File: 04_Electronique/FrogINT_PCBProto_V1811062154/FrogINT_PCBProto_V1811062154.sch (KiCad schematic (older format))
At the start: 35 parts, among them IC1 TTP223-BA6, J1 USB_B_Mini, J2 Conn_01x01_Female, J3 AVR-JTAG-10, Q1 PMV48XP, Q2 PMV48XP, U1 NCP1117-5.0_SOT223, U2 LP2985-3.3, U3 ATmega16U4RC-AU, Y1 16MHz

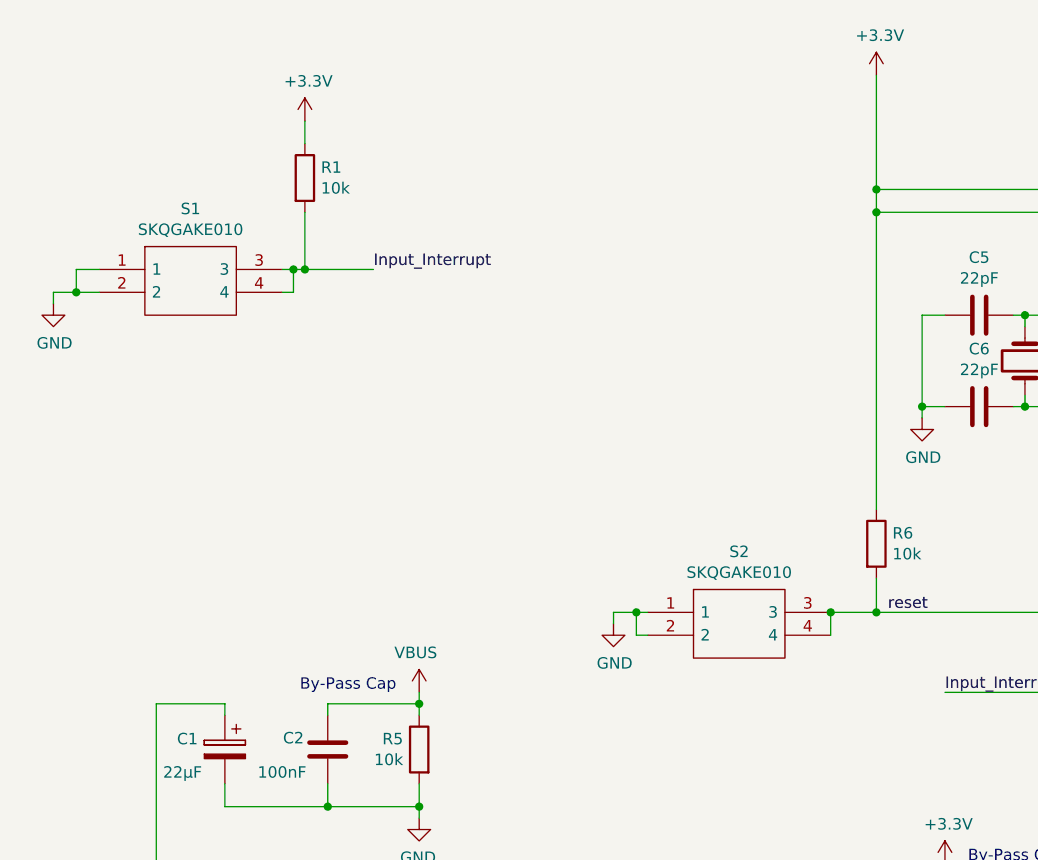
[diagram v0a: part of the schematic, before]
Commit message: 12/02/2019 : Remplacement des gros boutons par des plus petits
Impact :
	Mise à jour du fichier Excel FrogINT_BOM_V03-Commit-22-01-2019_RFQ_RS.xlsx suite à la mise à jour de la BOM (Attention pour les chiffrage en cours)
	Création des fichiers sources mécaniques pour ce nouveau Switch_PTS810SJG250SMTRLFS
	Mise à jour des références des librairies (pointeur).
	Déplacement partiel de la librairie SamacSys_Parts directement dans la "racine" du projet (et non plus dans l'arborescence C: etc.)
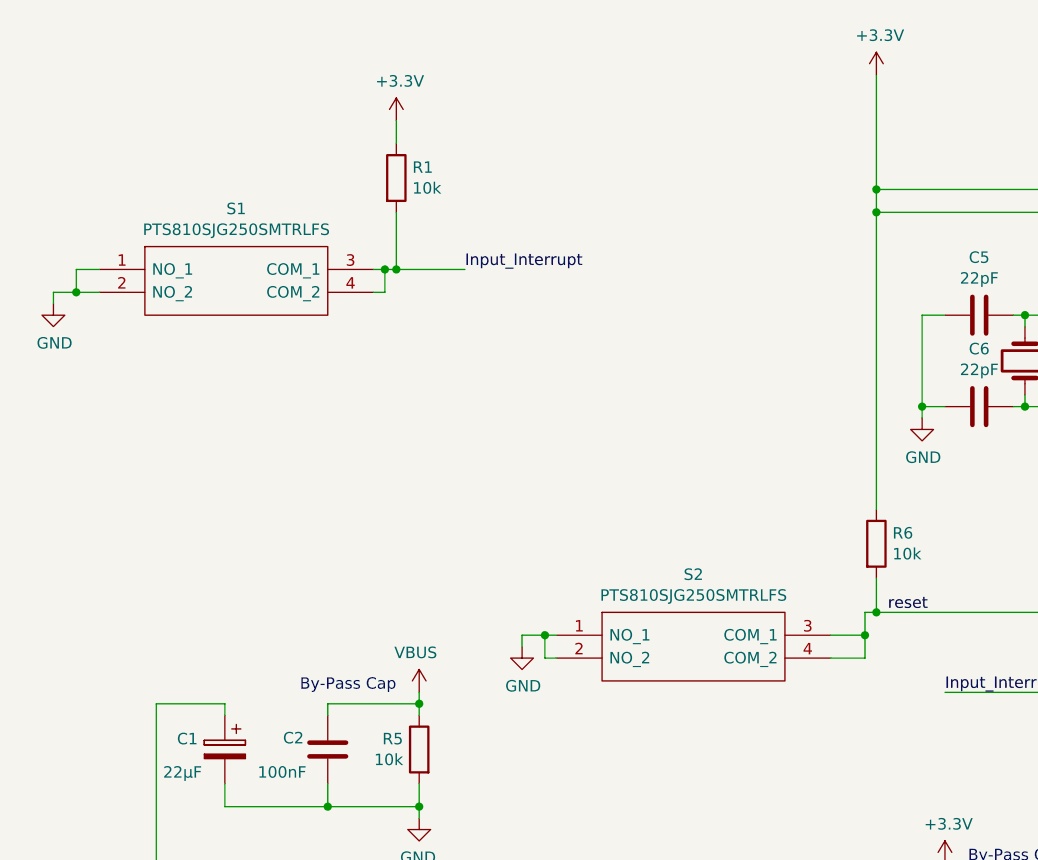
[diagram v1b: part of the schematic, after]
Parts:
- removed S1, S2: SKQGAKE010, SamacSys_Parts:SKQGAKE010, symbol FrogINT_PCBProto_V1811062154-rescue:SKQGAKE010-SamacSys_Parts
- added S1, S2: PTS810SJG250SMTRLFS, SamacSys_Parts:PTS810SJG250SMTRLFS, symbol SamacSys_Parts:PTS810SJG250SMTRLFS
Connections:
- net GND: now also S1.1 (NO_1), S1.2 (NO_2), S2.1 (NO_1), S2.2 (NO_2)
- net Input_Interrupt: now also S1.3 (COM_1), S1.4 (COM_2)
- net reset: now also S2.3 (COM_1), S2.4 (COM_2)
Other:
- moved on the sheet: R1
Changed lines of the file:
@@
 L power:GND #PWR012
 U 1 1 5BE239E3
-P 3200 3300
-F 0 "#PWR012" H 3200 3050 50  0001 C CNN
-F 1 "GND" H 3205 3127 50  0000 C CNN
-F 2 "" H 3200 3300 50  0001 C CNN
-F 3 "" H 3200 3300 50  0001 C CNN
-	1    3200 3300
-	1    0    0    -1
-$EndComp
-Wire Wire Line
-	3200 3300 3200 3250
-Wire Wire Line
-	3200 3250 3300 3250
+P 2800 3400
+F 0 "#PWR012" H 2800 3150 50  0001 C CNN
+F 1 "GND" H 2805 3227 50  0000 C CNN
+F 2 "" H 2800 3400 50  0001 C CNN
+F 3 "" H 2800 3400 50  0001 C CNN
+	1    2800 3400
+	1    0    0    -1
+$EndComp
+Wire Wire Line
+	2800 3400 2800 3350
+Wire Wire Line
+	2800 3350 2900 3350
 $Comp
 L Device:R R6
@@
 	5900 4800 5900 4750
 Wire Wire Line
-	4150 3250 4350 3250
-Wire Wire Line
 	4350 3100 4350 3250
-Connection ~ 4350 3250
 Wire Wire Line
 	4350 3250 5400 3250
@@
 L Device:R R1
 U 1 1 5BEA062B
-P 1850 1350
-F 0 "R1" H 1920 1396 50  0000 L CNN
-F 1 "10k" H 1920 1305 50  0000 L CNN
-F 2 "FTA_FrogINT_Library_Footprint_Package:R_0603_1608Metric" V 1780 1350 50  0001 C CNN
-F 3 "~" H 1850 1350 50  0001 C CNN
-	1    1850 1350
+P 2250 1350
+F 0 "R1" H 2320 1396 50  0000 L CNN
+F 1 "10k" H 2320 1305 50  0000 L CNN
+F 2 "FTA_FrogINT_Library_Footprint_Package:R_0603_1608Metric" V 2180 1350 50  0001 C CNN
+F 3 "~" H 2250 1350 50  0001 C CNN
+	1    2250 1350
 	1    0    0    -1
 $EndComp
@@
 L power:+3.3V #PWR04
 U 1 1 5BEA067C
-P 1850 1100
-F 0 "#PWR04" H 1850 950 50  0001 C CNN
-F 1 "+3.3V" H 1865 1273 50  0000 C CNN
-F 2 "" H 1850 1100 50  0001 C CNN
-F 3 "" H 1850 1100 50  0001 C CNN
-	1    1850 1100
-	1    0    0    -1
-$EndComp
-Wire Wire Line
-	1850 1100 1850 1200
-Wire Wire Line
-	1850 1500 1850 1750
+P 2250 1100
+F 0 "#PWR04" H 2250 950 50  0001 C CNN
+F 1 "+3.3V" H 2265 1273 50  0000 C CNN
+F 2 "" H 2250 1100 50  0001 C CNN
+F 3 "" H 2250 1100 50  0001 C CNN
+	1    2250 1100
+	1    0    0    -1
+$EndComp
+Wire Wire Line
+	2250 1100 2250 1200
+Wire Wire Line
+	2250 1500 2250 1750
 Text Label 4650 3600 0    50   ~ 0
 Input_Interrupt
 Wire Wire Line
 	5500 3600 4650 3600
-Text Label 2150 1750 0    50   ~ 0
+Text Label 2550 1750 0    50   ~ 0
 Input_Interrupt
 Wire Wire Line
-	1850 1750 2150 1750
+	2250 1750 2550 1750
 Wire Wire Line
 	6600 4350 9500 4350
@@
 $EndComp
 NoConn ~ 6600 2950
-$Comp
-L FrogINT_PCBProto_V1811062154-rescue:SKQGAKE010-SamacSys_Parts S1
-U 1 1 5C3DDA07
+Wire Wire Line
+	750  1850 850  1850
+Wire Wire Line
+	950  1750 850  1750
+Wire Wire Line
+	850  1750 850  1850
+Wire Wire Line
+	850  1850 950  1850
+Wire Wire Line
+	2250 1750 2200 1750
+Connection ~ 2250 1750
+Wire Wire Line
+	2150 1850 2200 1850
+Wire Wire Line
+	2200 1850 2200 1750
+Connection ~ 2200 1750
+Wire Wire Line
+	2200 1750 2150 1750
+Wire Wire Line
+	2950 3450 2900 3450
+Wire Wire Line
+	2900 3450 2900 3350
+Connection ~ 2900 3350
+Wire Wire Line
+	2900 3350 2950 3350
+$Comp
+L SamacSys_Parts:PTS810SJG250SMTRLFS S1
+U 1 1 5C636FCC
 P 950 1750
-F 0 "S1" H 1350 2015 50  0000 C CNN
-F 1 "SKQGAKE010" H 1350 1924 50  0000 C CNN
-F 2 "SamacSys_Parts:SKQGAKE010" H 1600 1850 50  0001 L CNN
-F 3 "http://uk.rs-online.com/webdocs/10d6/0900766b810d6137.pdf" H 1600 1750 50  0001 L CNN
-F 4 "Tact switch,SMT,SPST,with stem,3.43N o/f Stem Tactile Switch, SPST-NO 50 mA 1.5mm" H 1600 1650 50  0001 L CNN "Description"
-F 5 "" H 1600 1550 50  0001 L CNN "Height"
-F 6 "ALPS" H 1600 1450 50  0001 L CNN "Manufacturer_Name"
-F 7 "SKQGAKE010" H 1600 1350 50  0001 L CNN "Manufacturer_Part_Number"
-F 8 "7582076P" H 1600 1250 50  0001 L CNN "RS Part Number"
-F 9 "http://uk.rs-online.com/web/p/products/7582076P" H 1600 1150 50  0001 L CNN "RS Price/Stock"
-F 10 "688-SKQGAKE010" H 1600 1050 50  0001 L CNN "Mouser Part Number"
-F 11 "https://www.mouser.com/Search/Refine.aspx?Keyword=688-SKQGAKE010" H 1600 950 50  0001 L CNN "Mouser Price/Stock"
+F 0 "S1" H 1550 2015 50  0000 C CNN
+F 1 "PTS810SJG250SMTRLFS" H 1550 1924 50  0000 C CNN
+F 2 "SamacSys_Parts:PTS810SJG250SMTRLFS" H 2000 1850 50  0001 L CNN
+F 3 "https://www.ckswitches.com/media/1476/pts810.pdf" H 2000 1750 50  0001 L CNN
+F 4 "PTS810SJG250SMTRLFS (Tactile Switches) Switch Tactile N.O. SPST Button J-Bend 0.05A 16VDC 100000Cycles 3.92N SMD T/R" H 2000 1650 50  0001 L CNN "Description"
+F 5 "C & K COMPONENTS" H 2000 1450 50  0001 L CNN "Manufacturer_Name"
+F 6 "PTS810SJG250SMTRLFS" H 2000 1350 50  0001 L CNN "Manufacturer_Part_Number"
+F 7 "135-9492" H 2000 1250 50  0001 L CNN "RS Part Number"
+F 8 "611-PTS810SJG250SMTR" H 2000 1050 50  0001 L CNN "Mouser Part Number"
+F 9 "https://www.mouser.com/Search/Refine.aspx?Keyword=611-PTS810SJG250SMTR" H 2000 950 50  0001 L CNN "Mouser Price/Stock"
 	1    950  1750
 	1    0    0    -1
 $EndComp
-$Comp
-L FrogINT_PCBProto_V1811062154-rescue:SKQGAKE010-SamacSys_Parts S2
-U 1 1 5C3DDAF3
-P 3350 3250
-F 0 "S2" H 3750 3515 50  0000 C CNN
-F 1 "SKQGAKE010" H 3750 3424 50  0000 C CNN
-F 2 "SamacSys_Parts:SKQGAKE010" H 4000 3350 50  0001 L CNN
-F 3 "http://uk.rs-online.com/webdocs/10d6/0900766b810d6137.pdf" H 4000 3250 50  0001 L CNN
-F 4 "Tact switch,SMT,SPST,with stem,3.43N o/f Stem Tactile Switch, SPST-NO 50 mA 1.5mm" H 4000 3150 50  0001 L CNN "Description"
-F 5 "" H 4000 3050 50  0001 L CNN "Height"
-F 6 "ALPS" H 4000 2950 50  0001 L CNN "Manufacturer_Name"
-F 7 "SKQGAKE010" H 4000 2850 50  0001 L CNN "Manufacturer_Part_Number"
-F 8 "7582076P" H 4000 2750 50  0001 L CNN "RS Part Number"
-F 9 "http://uk.rs-online.com/web/p/products/7582076P" H 4000 2650 50  0001 L CNN "RS Price/Stock"
-F 10 "688-SKQGAKE010" H 4000 2550 50  0001 L CNN "Mouser Part Number"
-F 11 "https://www.mouser.com/Search/Refine.aspx?Keyword=688-SKQGAKE010" H 4000 2450 50  0001 L CNN "Mouser Price/Stock"
-	1    3350 3250
-	1    0    0    -1
-$EndComp
-Wire Wire Line
-	750  1850 850  1850
-Wire Wire Line
-	950  1750 850  1750
-Wire Wire Line
-	850  1750 850  1850
 Connection ~ 850  1850
-Wire Wire Line
-	850  1850 950  1850
-Wire Wire Line
-	1850 1750 1800 1750
-Connection ~ 1850 1750
-Wire Wire Line
-	1750 1850 1800 1850
-Wire Wire Line
-	1800 1850 1800 1750
-Connection ~ 1800 1750
-Wire Wire Line
-	1800 1750 1750 1750
-Wire Wire Line
-	4150 3350 4150 3250
-Connection ~ 4150 3250
-Wire Wire Line
-	3350 3350 3300 3350
-Wire Wire Line
-	3300 3350 3300 3250
-Connection ~ 3300 3250
-Wire Wire Line
-	3300 3250 3350 3250
+$Comp
+L SamacSys_Parts:PTS810SJG250SMTRLFS S2
+U 1 1 5C64EBFD
+P 2950 3350
+F 0 "S2" H 3550 3615 50  0000 C CNN
+F 1 "PTS810SJG250SMTRLFS" H 3550 3524 50  0000 C CNN
+F 2 "SamacSys_Parts:PTS810SJG250SMTRLFS" H 4000 3450 50  0001 L CNN
+F 3 "https://www.ckswitches.com/media/1476/pts810.pdf" H 4000 3350 50  0001 L CNN
+F 4 "PTS810SJG250SMTRLFS (Tactile Switches) Switch Tactile N.O. SPST Button J-Bend 0.05A 16VDC 100000Cycles 3.92N SMD T/R" H 4000 3250 50  0001 L CNN "Description"
+F 5 "C & K COMPONENTS" H 4000 3050 50  0001 L CNN "Manufacturer_Name"
+F 6 "PTS810SJG250SMTRLFS" H 4000 2950 50  0001 L CNN "Manufacturer_Part_Number"
+F 7 "135-9492" H 4000 2850 50  0001 L CNN "RS Part Number"
+F 8 "611-PTS810SJG250SMTR" H 4000 2650 50  0001 L CNN "Mouser Part Number"
+F 9 "https://www.mouser.com/Search/Refine.aspx?Keyword=611-PTS810SJG250SMTR" H 4000 2550 50  0001 L CNN "Mouser Price/Stock"
+	1    2950 3350
+	1    0    0    -1
+$EndComp
+Wire Wire Line
+	4150 3450 4300 3450
+Wire Wire Line
+	4300 3450 4300 3350
+Wire Wire Line
+	4300 3350 4150 3350
+Wire Wire Line
+	4300 3350 4300 3250
+Wire Wire Line
+	4300 3250 4350 3250
+Connection ~ 4300 3350
+Connection ~ 4350 3250
 $EndSCHEMATC
